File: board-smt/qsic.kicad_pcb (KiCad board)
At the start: 4 copper layers, 214.1 x 131.7 mm, 256 parts, among them CON1 SD 0, CON2 SD 1, P1 USB_A, P2 Indicator Panel, Q201 Dual_NMOS, Q202 Dual_NMOS, Q203 Dual_NMOS, Q204 Dual_NMOS, Q205 Dual_NMOS, Q206 Dual_NMOS, Q207 Dual_NMOS, Q208 Dual_NMOS, Q209 Dual_NMOS, Q210 Dual_NMOS, Q211 Dual_NMOS, Q212 Dual_NMOS, Q301 Dual_NMOS, Q302 Dual_NMOS, Q303 Dual_NMOS, Q304 Dual_NMOS, Q305 Dual_NMOS, Q306 Dual_NMOS, Q307 Dual_NMOS, Q308 Dual_NMOS, U201 CMP401, U202 CMP401, U203 CMP401, U204 CMP401, U205 CMP401, U206 CMP401, U301 CMP401, U302 CMP401, U303 CMP401, U304 CMP401, U305 CMP401, U306 AOZ3010PI, U307 AOZ3010PI, U308 RT8288A, U309 SC189, U401 XC7A75T-CSG324, U501 IS43TR16128B, U601 MAX3033E

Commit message: Updated to KiCad v5
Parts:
- removed P1: USB_A, Connect:USB_A
- added J601: USB_A, Connect:USB_A, F.Cu at (46.6, 97.8)
- added JTAG: TC2050-IDC-NL, TC2050-IDC-NL, F.Cu at (93.3, 47.4)
- added U602: USB3340, Housings_DFN_QFN:QFN-32-1EP_5x5mm_Pitch0.5mm, F.Cu at (62.0, 99.8)
- D301: value LED_Small_ALT -> Configure
- REF**: footprint myMods.pretty:DEC-Handle -> DEC-Handle
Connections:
- P2 pad 1: /I/O/IPlatch_P -> /I/O/IPdata_P
- P2 pad 10: /I/O/IPblank_N -> /I/O/IPclk_N
- P2 pad 2: /I/O/IPlatch_N -> /I/O/IPdata_N
- P2 pad 3: /I/O/IPdata_P -> GND
- P2 pad 4: /I/O/IPdata_N -> /I/O/IPlatch_P
- P2 pad 5: Net-(P2-Pad5) -> /I/O/IPlatch_N
- P2 pad 6: Net-(P2-Pad6) -> /I/O/IPblank_P
- P2 pad 7: /I/O/IPclk_P -> /I/O/IPblank_N
- P2 pad 8: /I/O/IPclk_N -> GND
- P2 pad 9: /I/O/IPblank_P -> /I/O/IPclk_P
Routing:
- net /BDAL11: track 26.3 -> 25.4 mm

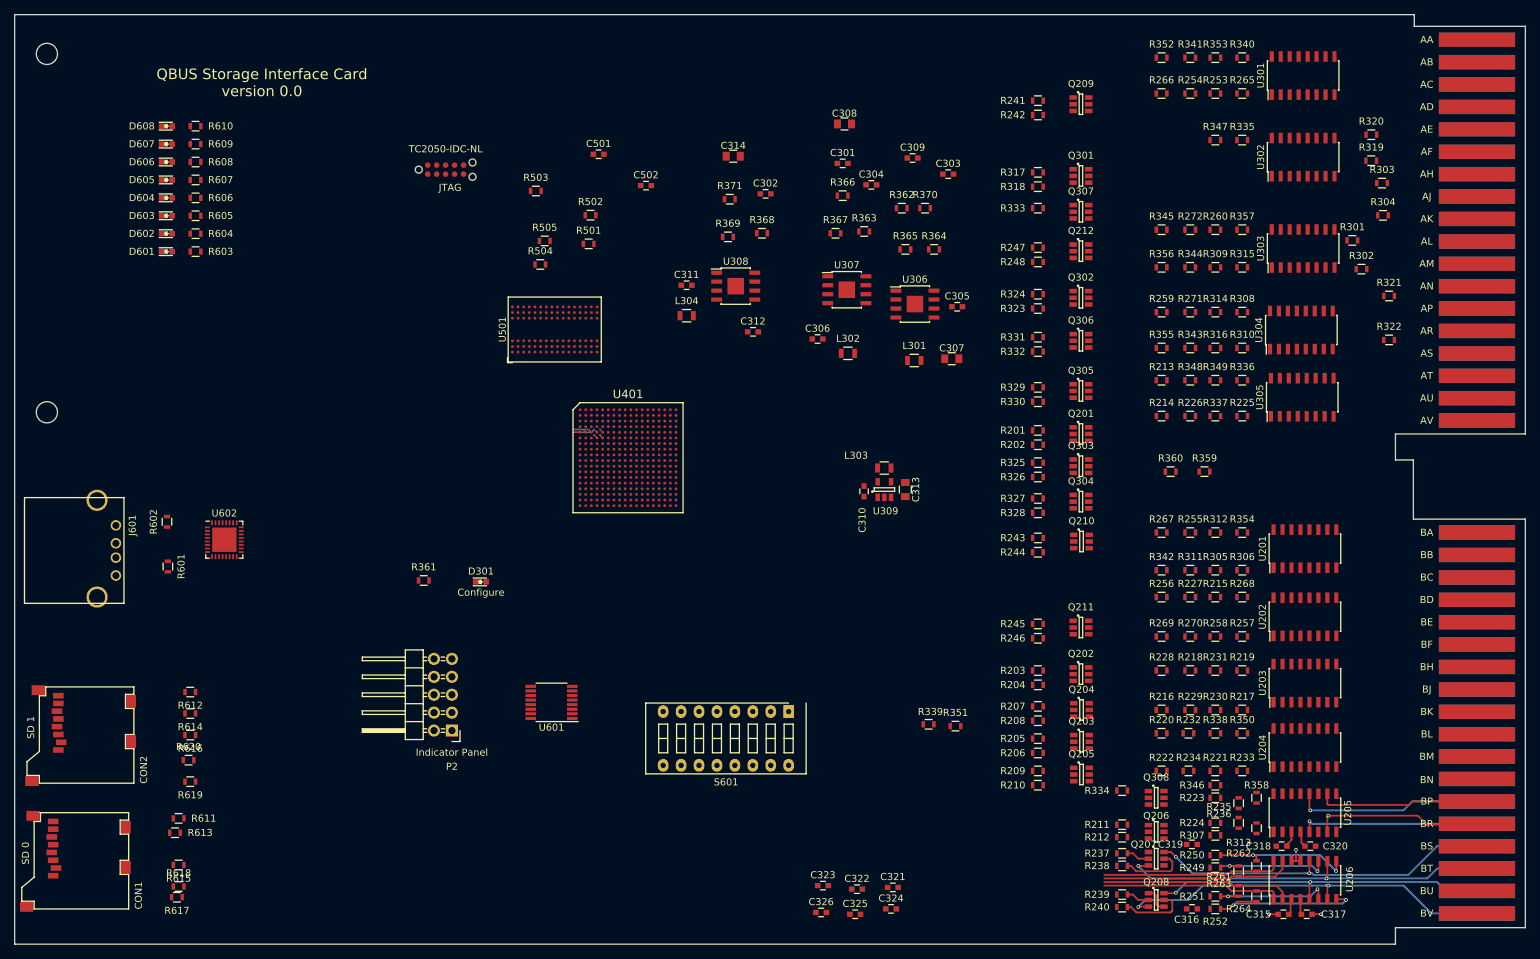
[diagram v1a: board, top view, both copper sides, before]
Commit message: These are all old changes in directories that are now historical.
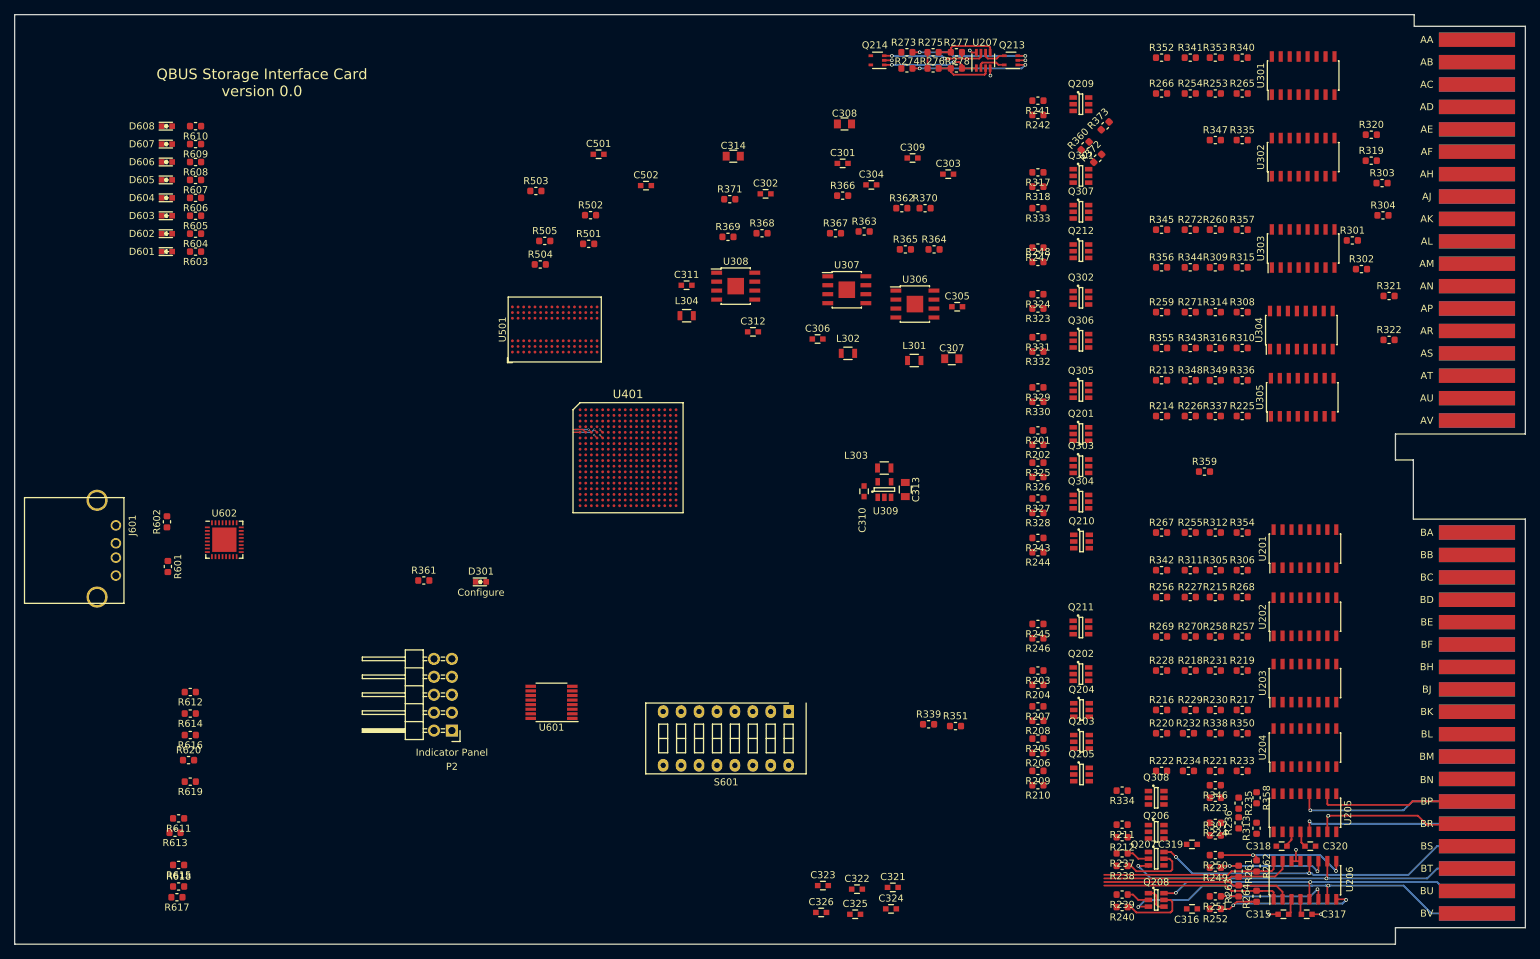
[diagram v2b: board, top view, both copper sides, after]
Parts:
- removed CON1: SD 0, myMods.pretty:microSD-3M-2900-series
- removed CON2: SD 1, myMods.pretty:microSD-3M-2900-series
- removed JTAG: TC2050-IDC-NL, TC2050-IDC-NL
- removed REF**: DEC Handle, DEC-Handle
- removed h1, h2: MountingHole_3mm, Mounting_Holes:MountingHole_3mm
- added Q213: DMN32, Package_TO_SOT_SMD:SOT-353_SC-70-5, F.Cu at (173.5, 31.9)
- added Q214: DMN32, Package_TO_SOT_SMD:SOT-353_SC-70-5, F.Cu at (154.6, 31.9)
- added R273: 66, Resistor_SMD:R_0603_1608Metric, F.Cu at (158.7, 30.7)
- added R274: 66, Resistor_SMD:R_0603_1608Metric, F.Cu at (158.7, 33.0)
- added R275: 20kΩ, Resistor_SMD:R_0603_1608Metric, F.Cu at (162.4, 30.7)
- added R276: 20kΩ, Resistor_SMD:R_0603_1608Metric, F.Cu at (162.4, 33.0)
- added R277: 340kΩ, Resistor_SMD:R_0603_1608Metric, F.Cu at (165.7, 30.7)
- added R278: 340kΩ, Resistor_SMD:R_0603_1608Metric, F.Cu at (165.7, 33.0)
- added R372: 20kΩ, Resistor_SMD:R_0603_1608Metric, F.Cu at (185.8, 45.8)
- added R373: 340kΩ, Resistor_SMD:R_0603_1608Metric, F.Cu at (186.8, 41.2)
- added U207: MAX9107, Package_TO_SOT_SMD:SOT-23-8, F.Cu at (169.5, 31.9)
- R201, R202, R203, R204, R205, R206, R207, R208, R209, R210, R211, R212, R213, R214, R215, R216, R217, R218, R219, R220, R221, R222, R223, R224, R225, R226, R227, R228, R229, R230, R231, R232, R233, R234, R235, R236, R237, R238, R239, R240, R241, R242, R243, R244, R245, R246, R247, R248, R249, R250, R251, R252, R253, R254, R255, R256, R257, R258, R259, R260, R261, R262, R263, R264, R265, R266, R267, R268, R269, R270, R271, R272, R301, R302, R303, R304, R305, R306, R307, R308, R309, R310, R311, R312, R313, R314, R315, R316, R317, R318, R319, R320, R321, R322, R323, R324, R325, R326, R327, R328, R329, R330, R331, R332, R333, R334, R335, R336, R337, R338, R339, R340, R341, R342, R343, R344, R345, R346, R347, R348, R349, R350, R351, R352, R353, R354, R355, R356, R357, R358, R359, R361, R362, R363, R364, R365, R366, R367, R368, R369, R370, R371, R501, R502, R503, R504, R505, R601, R602, R603, R604, R605, R606, R607, R608, R609, R610, R611, R612, R613, R614, R615, R616, R617, R618, R619, R620: footprint Resistors_SMD:R_0603 -> Resistor_SMD:R_0603_1608Metric
- R360: value 5kΩ -> R; footprint Resistors_SMD:R_0603 -> Resistor_SMD:R_0603_1608Metric
- moved R360 47.7 mm to (184.0, 44.0), turned to 45 degrees
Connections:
- Q307 pad 3: (no net) -> /Bus Control/BIRQ7
- Q307 pad 4: (no net) -> GND
- Q307 pad 5: (no net) -> Net-(Q307-Pad5)
- R360 pad 1: +1V5 -> Net-(Q307-Pad5)
- R360 pad 2: GND -> /TIRQ7
- U602 pad 30: (no net) -> Net-(U602-Pad30)
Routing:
- net Net-(Q213-Pad1): track 0.00 -> 17.3 mm, vias 0 -> 2
- net Net-(Q213-Pad3): track 0.00 -> 17.3 mm, vias 0 -> 2
- net Net-(Q214-Pad3): track 0.00 -> 16.3 mm, vias 0 -> 2
- net Net-(Q214-Pad1): track 0.00 -> 13.9 mm, vias 0 -> 2
- net Net-(R275-Pad2): track 0.00 -> 8.84 mm
- net Net-(R276-Pad2): track 0.00 -> 8.15 mm
- net /Bus Control/BIRQ6: track 0.00 -> 4.12 mm
- net /Bus Control/BIRQ5: track 0.00 -> 3.49 mm
- net GND: track 12.7 -> 16.0 mm, vias 4 -> 7
- net +1V5_ref: track 0.00 -> 2.29 mm
- net +5V: track 4.48 -> 5.53 mm, vias 0 -> 1
